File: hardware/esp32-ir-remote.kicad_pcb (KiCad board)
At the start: 2 copper layers, 80 x 55 mm, 76 parts, among them J2 USB_C_Receptacle_USB2.0_14P, J3 Qwiic_I2C, J4 GPIO_PWR, J5 EXT_IR, J6 JTAG, Q1 Q_NPN_BCE, Q2 Q_NPN_BCE, Q3 IRLML6344, Q4 2N7002, Q5 2N7002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

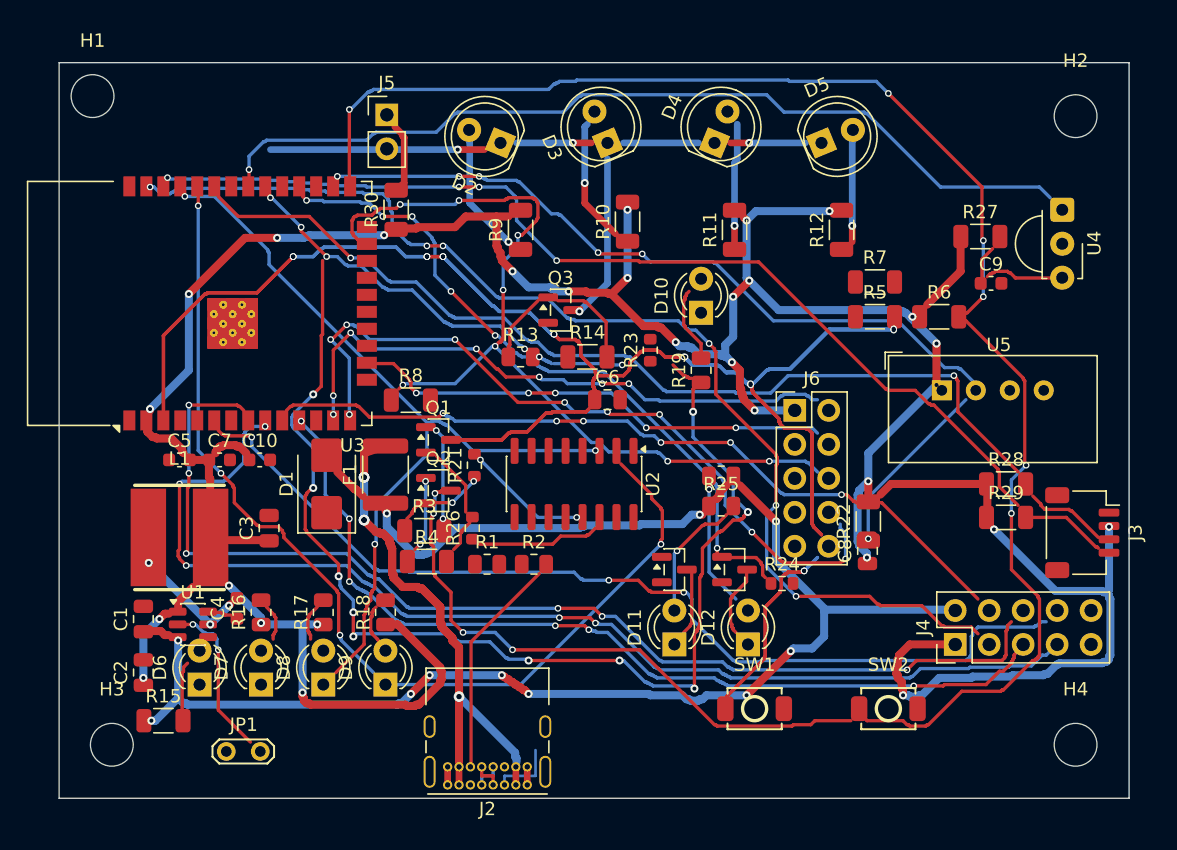
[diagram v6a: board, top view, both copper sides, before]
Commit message: H2.3: pours + stitching in; one real unconnected leg fixed (U1/3)
Key discovery: the router's 'unrouted legs' were mostly phantom - KiCad
connectivity showed trunk copper already touching those pads; the only true
gap was +5V->U1/3 (hand-routed via + stub). GND pour both layers + antenna
keepout + 57 stitching vias. DRC: 55 errors remaining (shorts 17, dangling
27, courtyards 4, hole_to_hole 6, clearance 7, thermal 12, keepout 2) -
all enumerated, surgical fixes in progress.
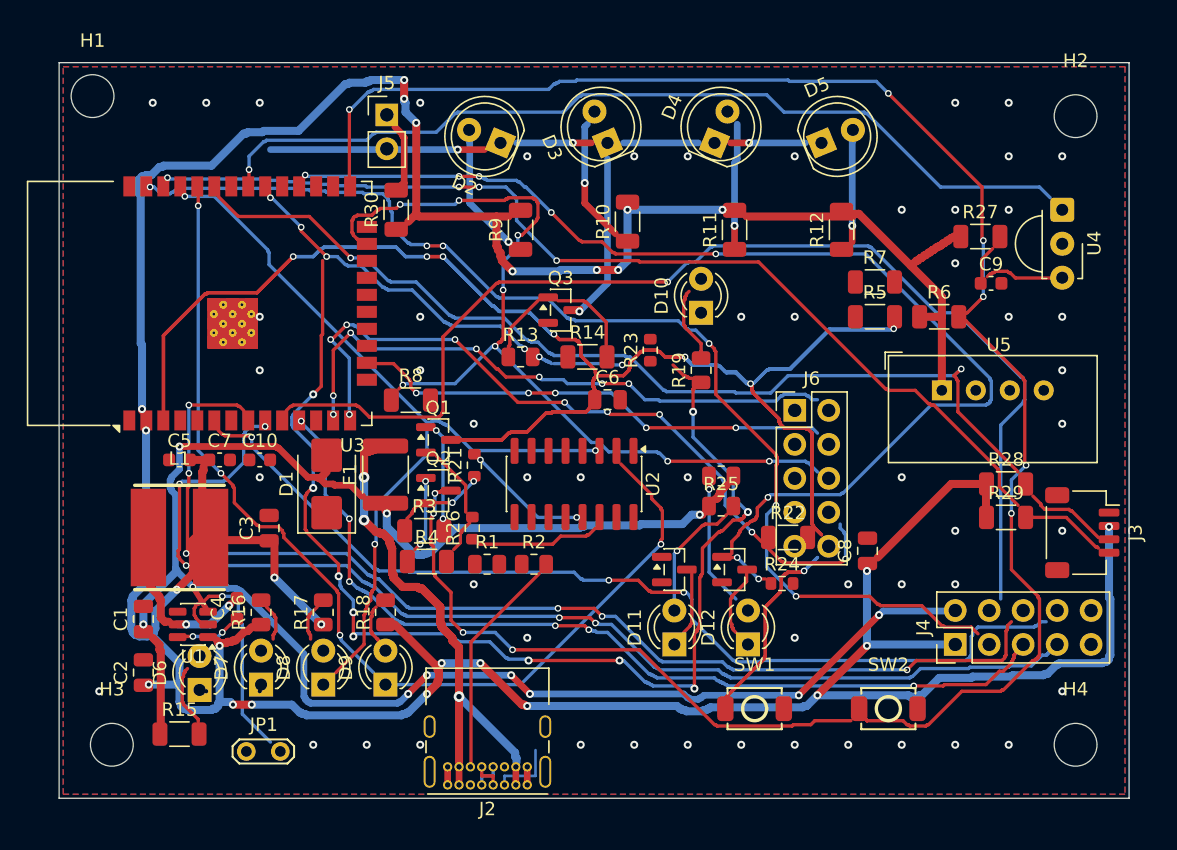
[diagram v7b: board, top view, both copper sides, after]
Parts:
- moved R22 6.12 mm to (154.5, 95.5), turned to 0 degrees
- moved R15 1.56 mm to (109.0, 110.2)
- moved JP1 1.50 mm to (114.0, 111.5)
- moved D6 0.40 mm to (110.5, 106.9)
- turned U1 to 180 degrees
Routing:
- net TEMP_DATA: track 67.3 -> 0.00 mm, vias 6 -> 0
- net +3.3V: track 232.4 -> 287.1 mm, vias 29 -> 25
- net USER_LED2: track 50.7 -> 87.7 mm, vias 6 -> 8
- net ESP_GPIO25: track 58.1 -> 85.7 mm, vias 6 -> 1
- net +5V: track 114.4 -> 135.6 mm
- net ESP_EN: track 223.5 -> 230.4 mm, vias 16 -> 8
- net ESP_GPIO0: track 157.2 -> 163.2 mm
- net Net-(JP1-B): track 11.5 -> 17.3 mm, vias 2 -> 1
- net ESP_GPIO22: track 83.2 -> 87.1 mm
- net Net-(F1-Pad2): track 60.2 -> 63.6 mm, vias 5 -> 3
- net Net-(U1-BST): track 1.08 -> 4.31 mm, vias 0 -> 2
- net ESP_GPIO33: track 85.9 -> 89.1 mm
- net ESP_GPIO26: track 69.0 -> 71.9 mm
- net IR_TX: track 118.3 -> 120.8 mm
- net Net-(D9-A): track 3.82 -> 5.92 mm
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- added copper zone on B.Cu, net GND
- added copper zone on F.Cu, net GND

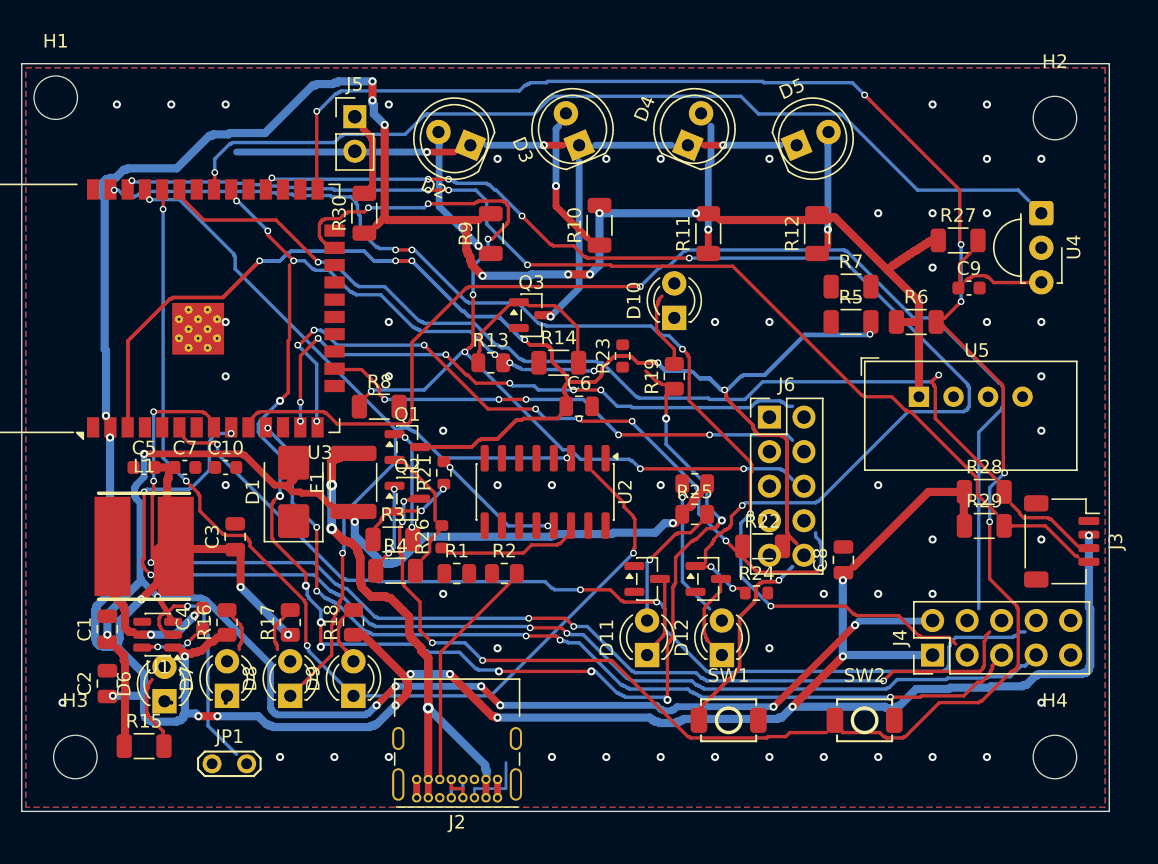
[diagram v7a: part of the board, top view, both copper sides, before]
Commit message: H2.3 WIP: post-finisher checkpoint (0 shorts; dangling/dups to clean)
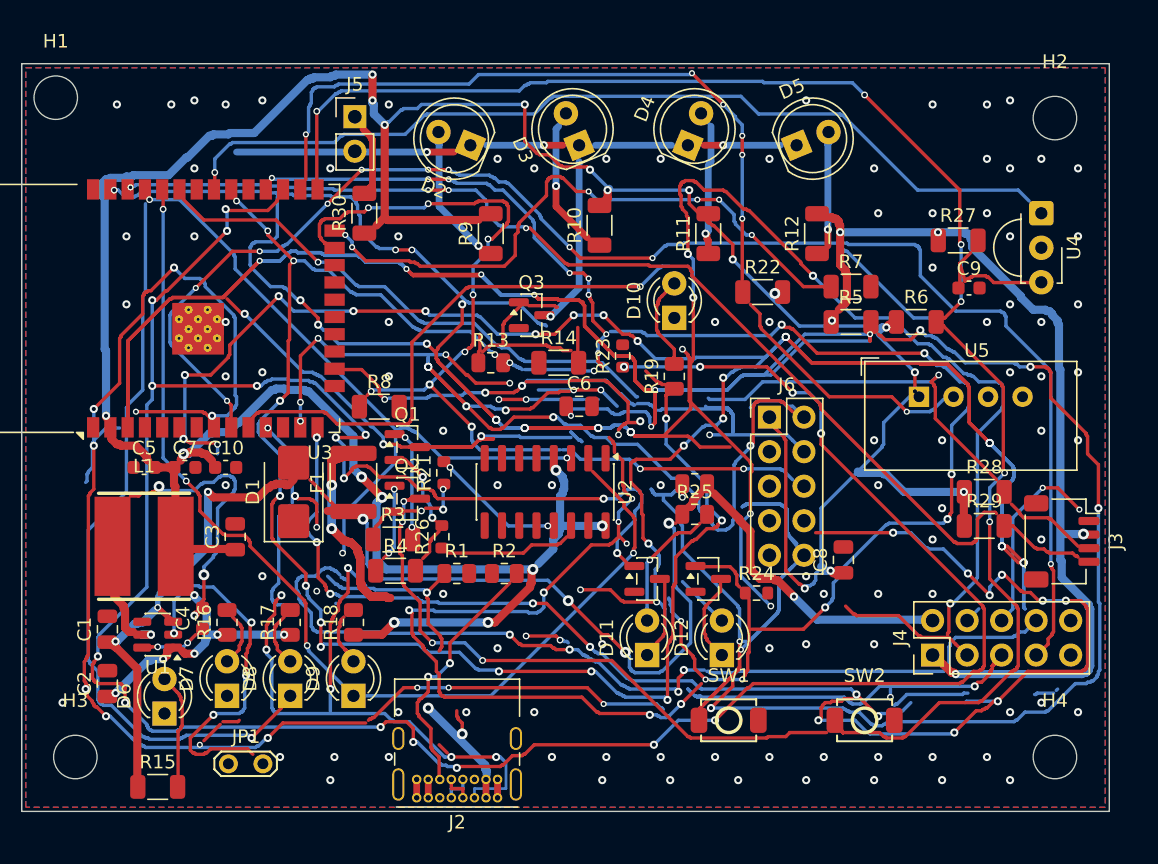
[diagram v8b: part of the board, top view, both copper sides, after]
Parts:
- moved R22 18.7 mm to (154.5, 76.8)
- moved R15 3.16 mm to (110.0, 113.2)
- moved JP1 1.20 mm to (115.2, 111.5)
- moved D6 0.90 mm to (110.5, 107.8)
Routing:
- net USER_LED1: track 0.00 -> 209.6 mm, vias 0 -> 21
- net ESP_GPIO34: track 72.7 -> 230.6 mm, vias 3 -> 28
- net ESP_GPIO23: track 85.6 -> 215.2 mm, vias 6 -> 22
- net ESP_EN: track 230.4 -> 340.1 mm, vias 8 -> 17
- net USER_LED2: track 87.7 -> 167.0 mm, vias 8 -> 23
- net TEMP_DATA: track 0.00 -> 70.4 mm, vias 0 -> 7
- net ESP_GPIO12: track 57.9 -> 115.6 mm, vias 9 -> 16
- net Net-(J2-CC1): track 4.92 -> 59.8 mm, vias 0 -> 7
- net ESP_GPIO32: track 83.5 -> 131.9 mm, vias 6 -> 14
- net ESP_GPIO14: track 45.4 -> 92.9 mm, vias 7 -> 13
- net ESP_GPIO2: track 0.00 -> 47.4 mm, vias 0 -> 6
- net UART_TX: track 60.8 -> 104.4 mm, vias 3 -> 4
- net ESP_GPIO25: track 85.7 -> 49.2 mm
- net +3.3V: track 287.1 -> 320.9 mm, vias 25 -> 35
- net +5V: track 135.6 -> 102.0 mm, vias 11 -> 8
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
